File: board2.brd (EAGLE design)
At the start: 100 x 80 mm, 75 parts, among them Q1 7.68M, Q2 16MHz

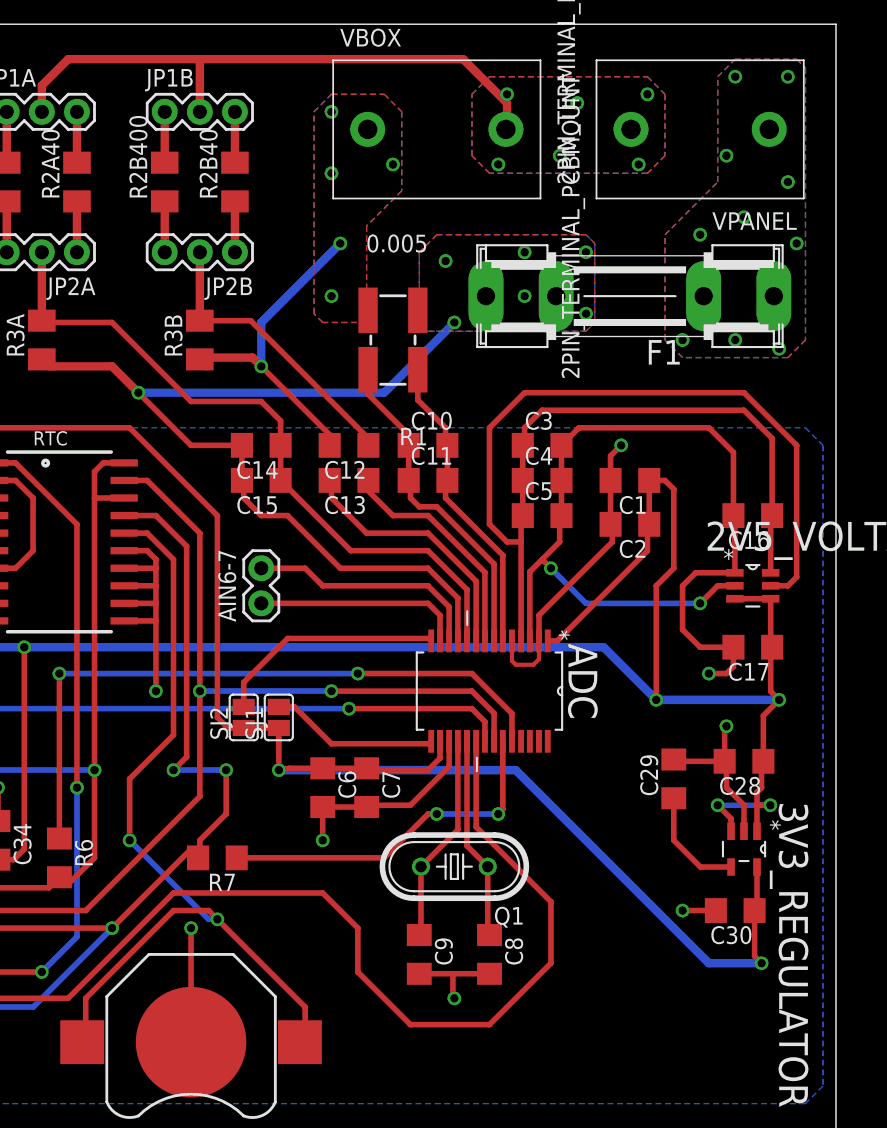
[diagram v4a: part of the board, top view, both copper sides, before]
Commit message: Fixed the fuse footprint
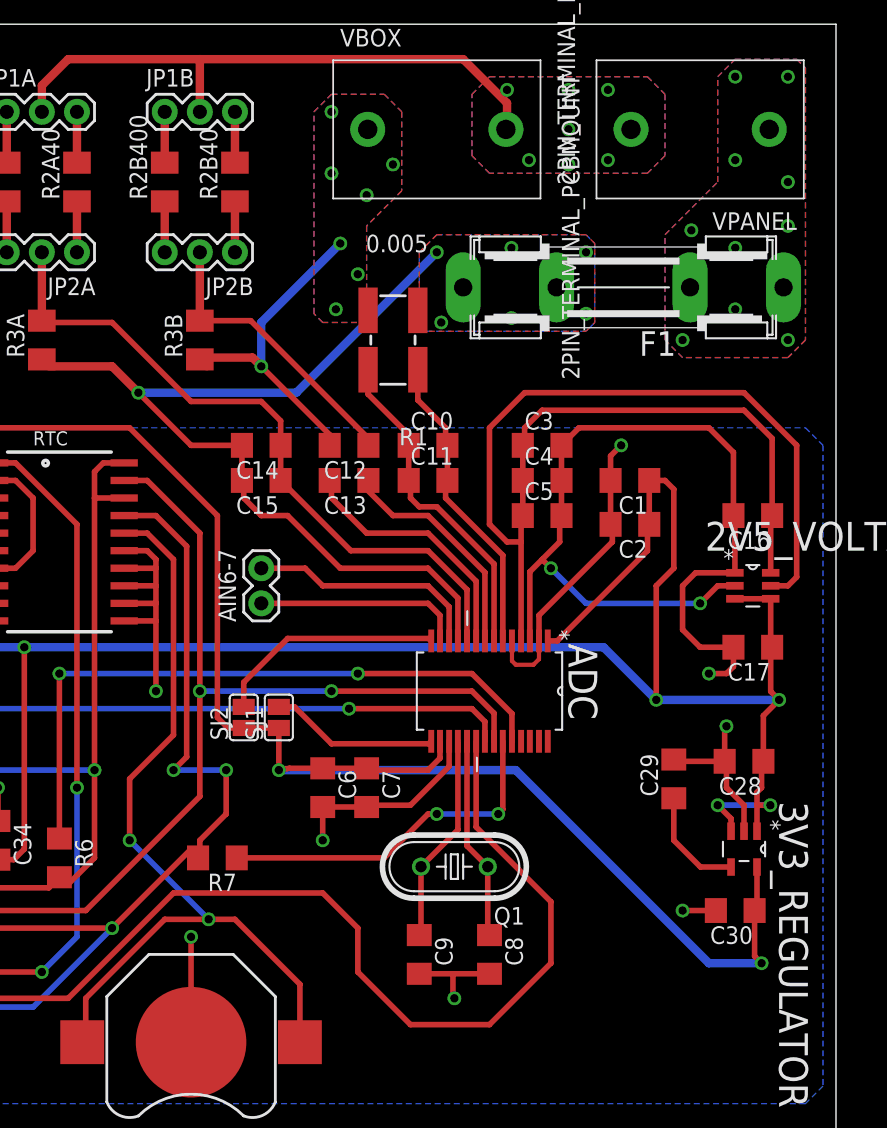
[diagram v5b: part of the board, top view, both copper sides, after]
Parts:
- F1: device fuse:SHK20L -> fuse:PAS_5X20
- moved F1 12.0 mm to (73.1, 61.0)
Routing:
- net N$15: track 62.0 -> 60.0 mm
- net AIN5: track 67.5 -> 68.3 mm
- net GND_ISO: track 263.7 -> 263.0 mm
- net VBUS1: vias 6 -> 7
- net AIN3: vias 6 -> 8
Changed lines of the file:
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@@
 <layer number="43" name="vRestrict" color="2" fill="10" visible="yes" active="yes"/>
 <layer number="44" name="Drills" color="7" fill="1" visible="no" active="yes"/>
-<layer number="45" name="Holes" color="7" fill="1" visible="no" active="yes"/>
+<layer number="45" name="Holes" color="7" fill="1" visible="yes" active="yes"/>
 <layer number="46" name="Milling" color="3" fill="1" visible="no" active="yes"/>
 <layer number="47" name="Measures" color="7" fill="1" visible="no" active="yes"/>
@@
 <attribute name="SUPPLIER" value="Analog Devices" x="25.4" y="52.07" size="1.778" layer="27" rot="R270" display="off"/>
 </element>
-<element name="F1" library="fuse" package="SHK20L" value="15A" x="85.09" y="60.325" rot="R180">
-<attribute name="MPN" value="" x="85.09" y="60.325" size="1.778" layer="27" rot="R180" display="off"/>
-<attribute name="OC_NEWARK" value="unknown" x="85.09" y="60.325" size="1.778" layer="27" rot="R180" display="off"/>
-<attribute name="MF" value="" x="85.09" y="60.325" size="1.778" layer="27" rot="R180" display="off"/>
-<attribute name="OC_FARNELL" value="unknown" x="85.09" y="60.325" size="1.778" layer="27" rot="R180" display="off"/>
-</element>
+<element name="F1" library="fuse" package="PAS_5X20" value="15A" x="73.0585" y="60.96" rot="R180"/>
 <element name="ICSP" library="SparkFun-Connectors" package="2X3" value="FEMALE 2x3" x="10.16" y="25.4" rot="R90">
 <attribute name="PROD_ID" value="CONN-11566" x="10.16" y="25.4" size="1.778" layer="27" rot="R90" display="off"/>
@@
 <vertex x="73.66" y="70.485"/>
 </polygon>
-<via x="76.2" y="74.93" extent="1-16" drill="0.6"/>
-<via x="86.36" y="74.93" extent="1-16" drill="0.6"/>
-<via x="85.725" y="69.85" extent="1-16" drill="0.6"/>
-<via x="81.28" y="74.295" extent="1-16" drill="0.6"/>
-<via x="80.01" y="70.485" extent="1-16" drill="0.6"/>
-<via x="75.565" y="69.85" extent="1-16" drill="0.6"/>
+<via x="76.2" y="75.2475" extent="1-16" drill="0.6"/>
+<via x="83.5025" y="75.2475" extent="1-16" drill="0.6"/>
+<via x="83.5025" y="70.1675" extent="1-16" drill="0.6"/>
+<via x="80.645" y="75.2475" extent="1-16" drill="0.6"/>
+<via x="80.645" y="69.85" extent="1-16" drill="0.6"/>
+<via x="77.7875" y="70.1675" extent="1-16" drill="0.6"/>
+<via x="80.645" y="72.39" extent="1-16" drill="0.6"/>
 </signal>
 <signal name="N$2">
@@
 <via x="67.945" y="69.85" extent="1-16" drill="0.6"/>
 <via x="63.5" y="69.215" extent="1-16" drill="0.6"/>
-<via x="63.5" y="60.325" extent="1-16" drill="0.6"/>
+<via x="63.8175" y="59.3725" extent="1-16" drill="0.6"/>
 <wire x1="63.37" y1="49.53" x2="63.37" y2="46.99" width="0" layer="19" extent="1-1"/>
+<via x="66.04" y="67.6275" extent="1-16" drill="0.6"/>
+<via x="65.405" y="61.9125" extent="1-16" drill="0.6"/>
 </signal>
 <signal name="AIN5">
@@
 <wire x1="43.05" y1="55.245" x2="42.545" y2="55.75" width="0.4064" layer="1"/>
 <via x="49.53" y="53.34" extent="1-16" drill="0.6"/>
-<wire x1="49.53" y1="53.34" x2="67.31" y2="53.34" width="0.6096" layer="16"/>
 <wire x1="43.05" y1="55.245" x2="47.625" y2="55.245" width="0.6096" layer="1"/>
 <wire x1="47.625" y1="55.245" x2="49.53" y2="53.34" width="0.6096" layer="1"/>
@@
 <vertex x="69.85" y="57.785"/>
 </polygon>
-<via x="77.47" y="63.5" extent="1-16" drill="0.6"/>
-<via x="72.39" y="58.42" extent="1-16" drill="0.6"/>
+<via x="76.5175" y="63.8175" extent="1-16" drill="0.6"/>
+<via x="71.4375" y="58.42" extent="1-16" drill="0.6"/>
 <via x="81.915" y="63.5" extent="1-16" drill="0.6"/>
 <via x="81.915" y="59.055" extent="1-16" drill="0.6"/>
-<via x="77.47" y="60.325" extent="1-16" drill="0.6"/>
-<wire x1="67.31" y1="53.34" x2="72.39" y2="58.42" width="0.6096" layer="16"/>
-<via x="71.755" y="62.865" extent="1-16" drill="0.6"/>
+<via x="76.5175" y="58.7375" extent="1-16" drill="0.6"/>
+<via x="71.12" y="63.5" extent="1-16" drill="0.6"/>
+<wire x1="49.53" y1="53.34" x2="60.96" y2="53.34" width="0.6096" layer="16"/>
+<wire x1="60.96" y1="53.34" x2="71.12" y2="63.5" width="0.6096" layer="16"/>
 </signal>
 <signal name="VBUS2">
@@
 <via x="92.71" y="76.2" extent="1-16" drill="0.6"/>
 <via x="96.52" y="76.2" extent="1-16" drill="0.6"/>
-<via x="92.075" y="70.485" extent="1-16" drill="0.6"/>
+<via x="92.71" y="70.1675" extent="1-16" drill="0.6"/>
 <via x="96.52" y="68.58" extent="1-16" drill="0.6"/>
-<via x="97.155" y="64.135" extent="1-16" drill="0.6"/>
-<via x="93.345" y="66.04" extent="1-16" drill="0.6"/>
-<via x="90.17" y="64.77" extent="1-16" drill="0.6"/>
-<via x="92.71" y="57.15" extent="1-16" drill="0.6"/>
+<via x="96.52" y="65.405" extent="1-16" drill="0.6"/>
+<via x="92.71" y="63.8175" extent="1-16" drill="0.6"/>
+<via x="89.535" y="65.0875" extent="1-16" drill="0.6"/>
+<via x="92.71" y="59.3725" extent="1-16" drill="0.6"/>
 <via x="88.9" y="57.15" extent="1-16" drill="0.6"/>
-<via x="95.885" y="56.515" extent="1-16" drill="0.6"/>
+<via x="96.52" y="57.15" extent="1-16" drill="0.6"/>
 </signal>
 <signal name="AIN1">
@@
 <via x="36.83" y="24.13" extent="1-16" drill="0.6"/>
 <contactref element="BAT1" pad="GND"/>
-<wire x1="53.34" y1="6.35" x2="53.34" y2="14.605" width="0.4064" layer="1"/>
-<via x="53.34" y="14.605" extent="1-16" drill="0.6"/>
+<wire x1="53.34" y1="6.35" x2="53.34" y2="13.97" width="0.4064" layer="1"/>
+<via x="53.34" y="13.97" extent="1-16" drill="0.6"/>
 <polygon width="0.4064" layer="1" thermals="no">
 <vertex x="20.955" y="48.26"/>
@@
 <contactref element="2V5_VOLTAGE_REF" pad="5"/>
 </signal>
-<signal name="N$22">
-<wire x1="45.72" y1="6.35" x2="45.72" y2="9.525" width="0.4064" layer="1"/>
-<wire x1="45.72" y1="9.525" x2="52.07" y2="15.875" width="0.4064" layer="1"/>
+<signal name="N$15">
+<wire x1="45.72" y1="7.62" x2="45.72" y2="9.525" width="0.4064" layer="1"/>
+<wire x1="45.72" y1="9.525" x2="51.435" y2="15.24" width="0.4064" layer="1"/>
 <contactref element="BAT1" pad="PWR@1"/>
 <contactref element="RTC" pad="16"/>
@@
 <via x="48.895" y="20.955" extent="1-16" drill="0.6"/>
 <wire x1="48.895" y1="20.955" x2="54.61" y2="15.24" width="0.4064" layer="16"/>
-<wire x1="55.245" y1="15.24" x2="61.595" y2="8.89" width="0.4064" layer="1"/>
-<wire x1="61.595" y1="8.89" x2="61.595" y2="6.731" width="0.4064" layer="1"/>
-<wire x1="61.595" y1="6.731" x2="61.214" y2="6.35" width="0.4064" layer="1"/>
-<wire x1="54.61" y1="15.24" x2="55.245" y2="15.24" width="0.4064" layer="16"/>
-<via x="55.245" y="15.24" extent="1-16" drill="0.6"/>
-<wire x1="52.07" y1="15.875" x2="54.61" y2="15.875" width="0.4064" layer="1"/>
-<wire x1="54.61" y1="15.875" x2="55.245" y2="15.24" width="0.4064" layer="1"/>
+<wire x1="61.214" y1="6.35" x2="61.214" y2="10.541" width="0.4064" layer="1"/>
+<wire x1="61.214" y1="10.541" x2="56.515" y2="15.24" width="0.4064" layer="1"/>
+<wire x1="56.515" y1="15.24" x2="54.61" y2="15.24" width="0.4064" layer="1"/>
+<via x="54.61" y="15.24" extent="1-16" drill="0.6"/>
+<wire x1="51.435" y1="15.24" x2="54.61" y2="15.24" width="0.4064" layer="1"/>
 </signal>
 </signals>

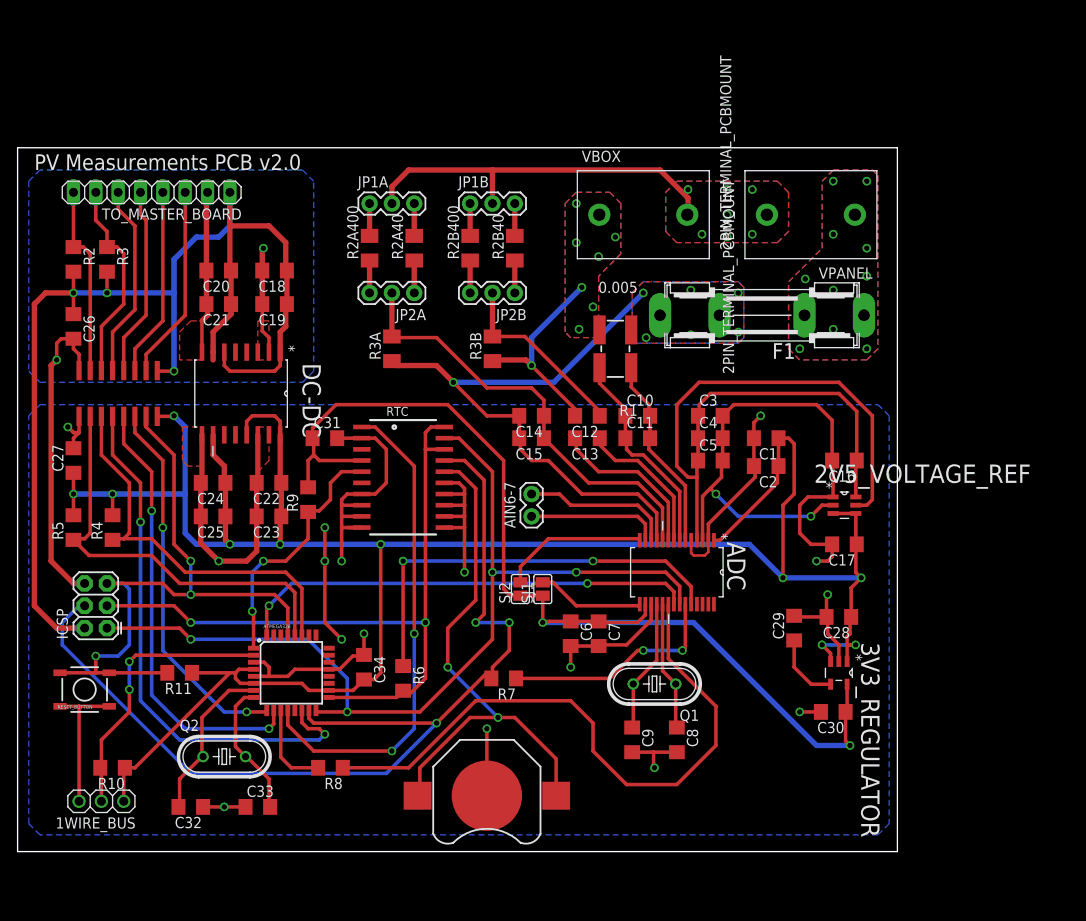
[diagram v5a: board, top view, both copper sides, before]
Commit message: Added: connector bypassing isolation, mounting holes
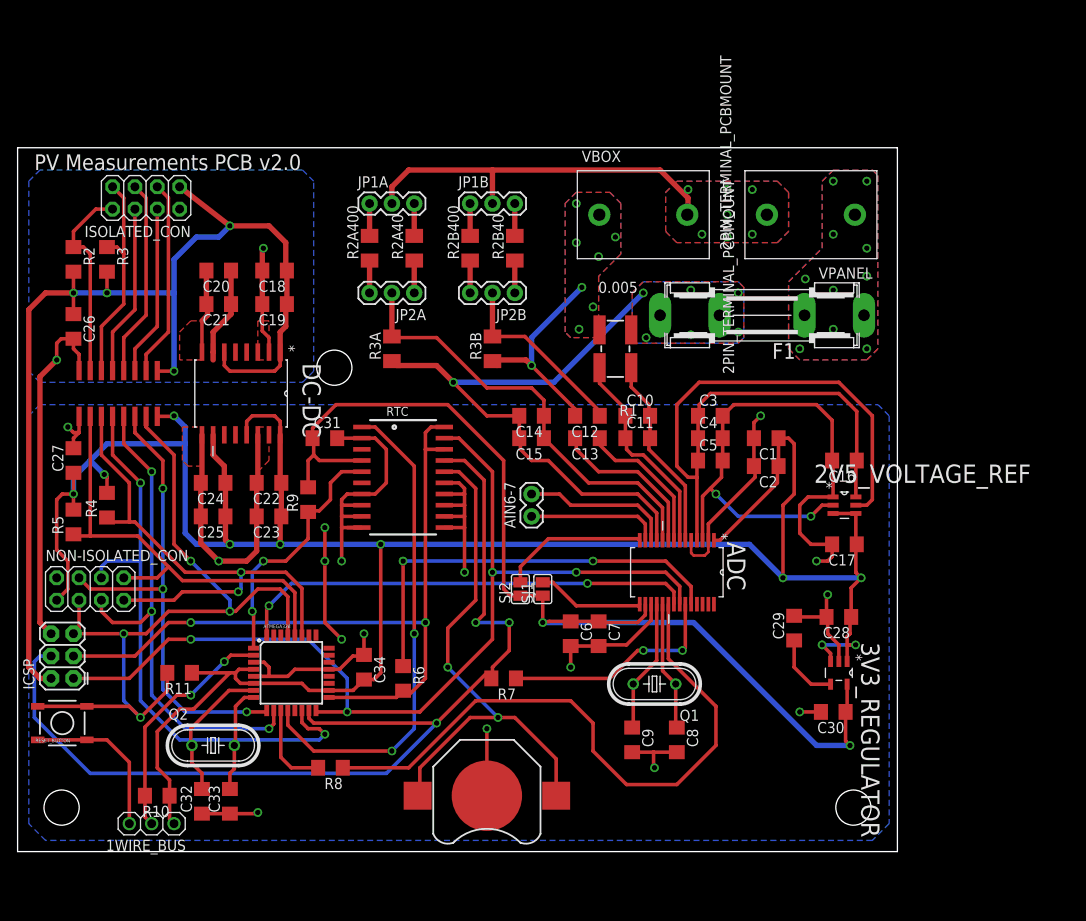
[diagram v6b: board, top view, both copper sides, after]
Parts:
- removed TO_MASTER_BOARD: (no value), pinhead:1X08
- added ISOLATED_CON, NON-ISOLATED_CON: (no value), adafruit:2X04
- moved ICSP 6.87 mm to (6.35, 19.7)
- moved 1WIRE_BUS 6.25 mm to (15.2, 3.17)
- moved R10 5.99 mm to (15.9, 6.35)
- moved RESET_BUTTON 4.58 mm to (5.08, 14.6)
- moved C33 3.24 mm to (24.1, 5.71), turned to 90 degrees
- moved R4 2.62 mm to (10.2, 39.4)
- moved Q2 1.80 mm to (22.2, 12.1)
- moved C32 1.42 mm to (21.0, 5.71), turned to 90 degrees
- moved R5 0.64 mm to (6.35, 37.5)
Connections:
- net 5V: now also ISOLATED_CON.1; no longer TO_MASTER_BOARD.1
- net 5V_ISO: now also NON-ISOLATED_CON.1
- net GND: now also ISOLATED_CON.2; no longer TO_MASTER_BOARD.2
- net GND_ISO: now also NON-ISOLATED_CON.2
- net IN1: now also ISOLATED_CON.3; no longer TO_MASTER_BOARD.3
- net IN2: now also ISOLATED_CON.4; no longer TO_MASTER_BOARD.4
- net IN2_ISO: now also NON-ISOLATED_CON.4
- net OUT1: now also ISOLATED_CON.5; no longer TO_MASTER_BOARD.5
- net OUT1_ISO: now also NON-ISOLATED_CON.5
- net OUT2: now also ISOLATED_CON.6; no longer TO_MASTER_BOARD.6
- net OUT2_ISO: now also NON-ISOLATED_CON.6
- net RESET: now also NON-ISOLATED_CON.3
- net SCL: now also ISOLATED_CON.8; no longer TO_MASTER_BOARD.8
- net SCL_ISO: now also NON-ISOLATED_CON.8
- net SDA: now also ISOLATED_CON.7; no longer TO_MASTER_BOARD.7
- net SDA_ISO: now also NON-ISOLATED_CON.7
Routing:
- net 5V_ISO: track 270.1 -> 291.7 mm
- net RESET: track 74.7 -> 90.2 mm, vias 3 -> 4
- net SDA_ISO: track 44.7 -> 59.9 mm, vias 0 -> 2
- net IN2_ISO: track 42.7 -> 55.3 mm, vias 2 -> 3
- net OUT1_ISO: track 50.2 -> 58.2 mm, vias 2 -> 3
- net OUT2_ISO: track 61.2 -> 67.2 mm
- net MISO: track 107.1 -> 112.2 mm
- net SCL_ISO: track 48.0 -> 53.0 mm
- net 1WIRE_BUS: track 31.7 -> 27.0 mm
- net SCLK: track 81.7 -> 86.3 mm
- net GND: track 66.6 -> 62.1 mm
- net GND_ISO: track 263.0 -> 266.7 mm
- net N$6: track 15.6 -> 12.1 mm
- net OUT2: track 22.1 -> 19.4 mm
- net MOSI: track 114.4 -> 116.8 mm
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
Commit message: Finished v2.2
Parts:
- removed 1WIRE_BUS: (no value), adafruit:1X03
- removed RESET_BUTTON: TAC_SWITCHSMD, SparkFun-Retired:TACTILE-SWITCH-SMD
- removed SJ1, SJ2: (no value), jumper:SJ
- added 1WIRE-BUS: PHOENIX-TERMINAL-3PIN, Paschalis_connectors:PHOENIX-TERMINAL-3PIN
- added RESET: TAC_SWITCHSMD, SparkFun-Retired:TACTILE-SWITCH-SMD
- added SJ1-RST, SJ2-SYNC: (no value), jumper:SJ
- moved R10 13.4 mm to (29.2, 5.08), turned to 90 degrees
- moved R8 7.67 mm to (42.5, 12.7)
- moved ICSP 2.01 mm to (6.99, 17.8)
- moved R9 1.42 mm to (33.7, 41.3)
- moved Q2 1.27 mm to (22.2, 10.8)
- moved JP1A 0.64 mm to (39.4, 73.7)
- moved R2A400 0.64 mm to (39.4, 68.6)
- moved R3A 0.64 mm to (41.9, 57.1)
- moved C32 0.63 mm to (20.3, 5.71)
- moved JP2A 0.63 mm to (44.5, 63.5)
- moved R2A40 0.63 mm to (44.5, 68.6)
- moved F1 0.32 mm to (73.4, 61.0)
- renumbered 2V5_VOLTAGE_REF to ADR3425, 3V3_REGULATOR to LP2985, ADC to ADS1256, DC-DC to ADUM5000, RTC to DS3234, SIGNAL_ISOLATOR to MAX14850
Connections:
- net 1WIRE_BUS: now also 1WIRE-BUS.2; no longer 1WIRE_BUS.2
- net 3V3: now also SJ1-RST.1, SJ2-SYNC.1; no longer SJ1.1, SJ2.1
- net 5V_ISO: now also 1WIRE-BUS.1; no longer 1WIRE_BUS.1
- net GND_ISO: now also 1WIRE-BUS.3, RESET.1, RESET.2; no longer 1WIRE_BUS.3, RESET_BUTTON.1, RESET_BUTTON.2
- net N$17: now also SJ1-RST.2; no longer SJ1.2
- net N$20: now also SJ2-SYNC.2; no longer SJ2.2
- net RESET: now also RESET.3, RESET.4; no longer RESET_BUTTON.3, RESET_BUTTON.4
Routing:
- net 5V_ISO: track 291.7 -> 317.3 mm, vias 10 -> 12
- net 1WIRE_BUS: track 27.0 -> 51.6 mm
- net N$16: track 71.5 -> 57.8 mm
- net 5V: track 140.2 -> 148.3 mm
- net N$20: track 16.7 -> 10.6 mm
- net GND: track 62.1 -> 68.2 mm, vias 2 -> 3
- net ADC_CS: track 10.0 -> 15.4 mm
- net 3V3: track 122.1 -> 126.3 mm
- net GND_ISO: track 266.7 -> 269.9 mm, vias 16 -> 19
- net AIN2: track 37.9 -> 40.4 mm
- net MOSI: track 116.8 -> 118.2 mm
- net N$17: track 12.2 -> 10.9 mm
- net GND_SENSE: track 15.8 -> 14.9 mm
- net RESET: track 90.2 -> 89.6 mm
- net AIN5: track 68.3 -> 68.9 mm
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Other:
- board text added: "*"
- board text added: "BATTERY 3V"
- board text added: "KULEUVEN - IMEC"
- board text added: "PV Measurement PCB"
- board text added: "v2.2 - March 2016 - Paschalis Sideridis"
- board text removed: "PV Measurements PCB v2.0"
